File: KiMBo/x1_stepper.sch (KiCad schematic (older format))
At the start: 23 parts, among them U25 TMC2130

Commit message: Arrange connectors and E-stepper circuit
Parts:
- R193: footprint Resistors_SMD:R_0805 -> Resistors_SMD:R_0603
- R195: footprint Resistors_SMD:R_0603 -> Resistors_SMD:R_0805
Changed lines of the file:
@@
 F 0 "R195" H 10700 6650 50  0000 R CNN
 F 1 "220mΩ" H 10700 6750 50  0000 R CNN
-F 2 "Resistors_SMD:R_0603" V 10680 6700 50  0001 C CNN
+F 2 "Resistors_SMD:R_0805" V 10680 6700 50  0001 C CNN
 F 3 "" H 10750 6700 50  0000 C CNN
 	1    10750 6700
@@
 F 0 "R193" V 9250 6900 50  0000 C CNN
 F 1 "4.75kΩ" V 9350 6900 50  0000 C CNN
-F 2 "Resistors_SMD:R_0805" V 9380 6900 50  0001 C CNN
+F 2 "Resistors_SMD:R_0603" V 9380 6900 50  0001 C CNN
 F 3 "" H 9450 6900 50  0000 C CNN
 	1    9450 6900

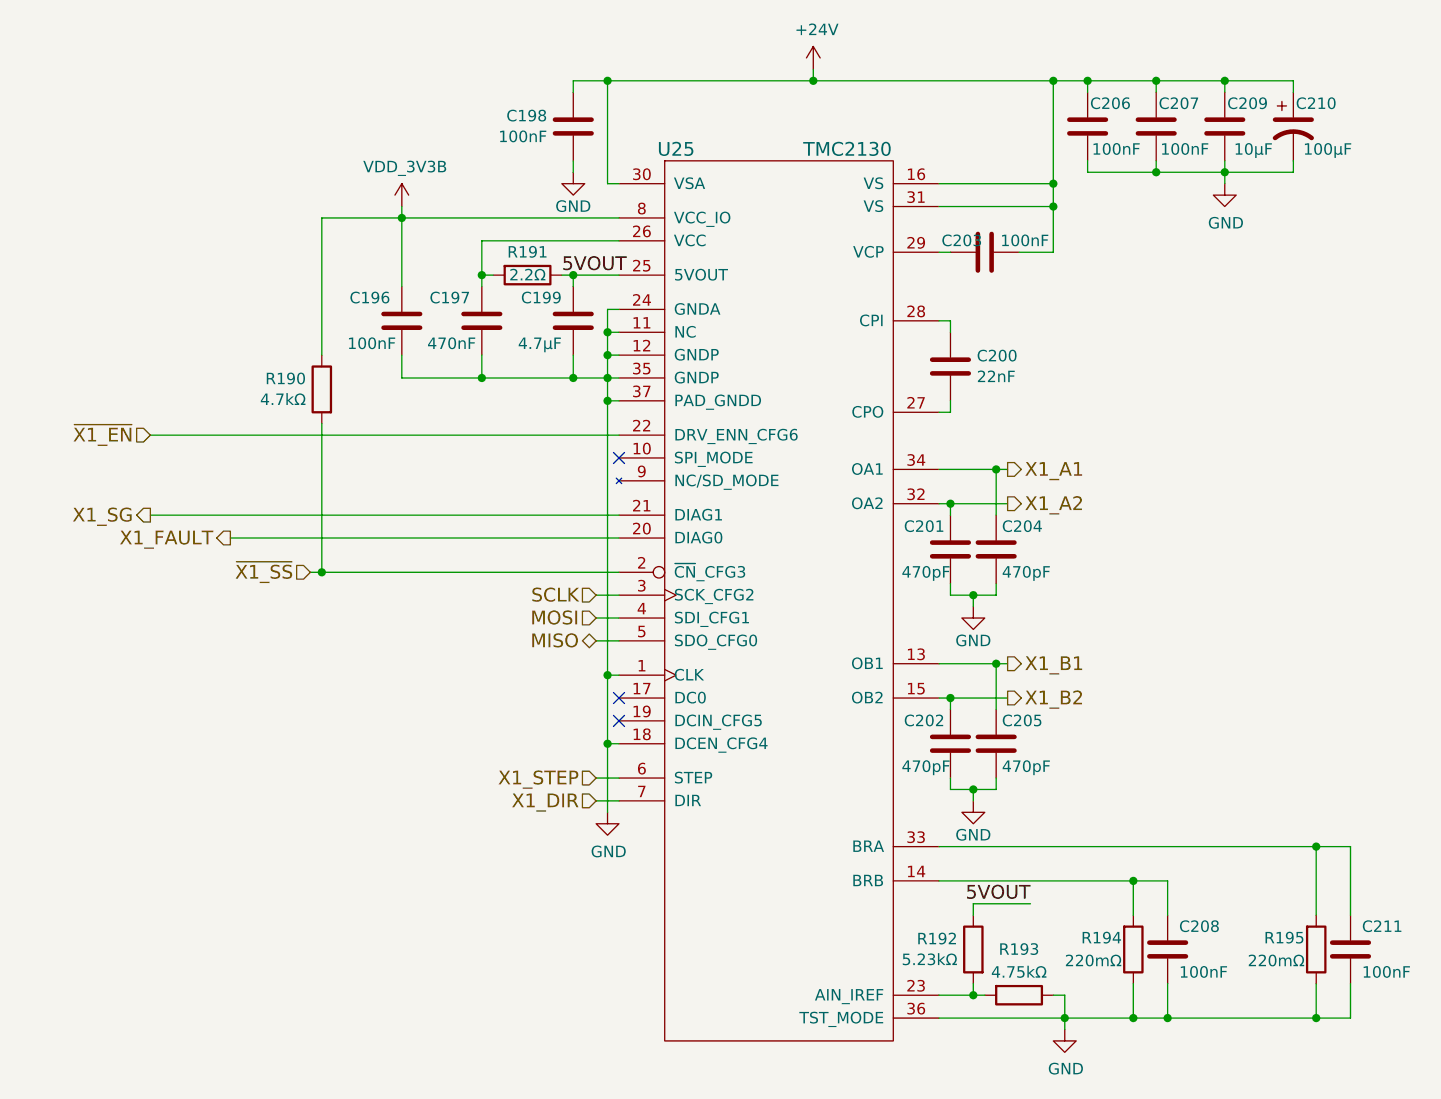
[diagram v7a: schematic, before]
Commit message: Remove HDMI from the schematic
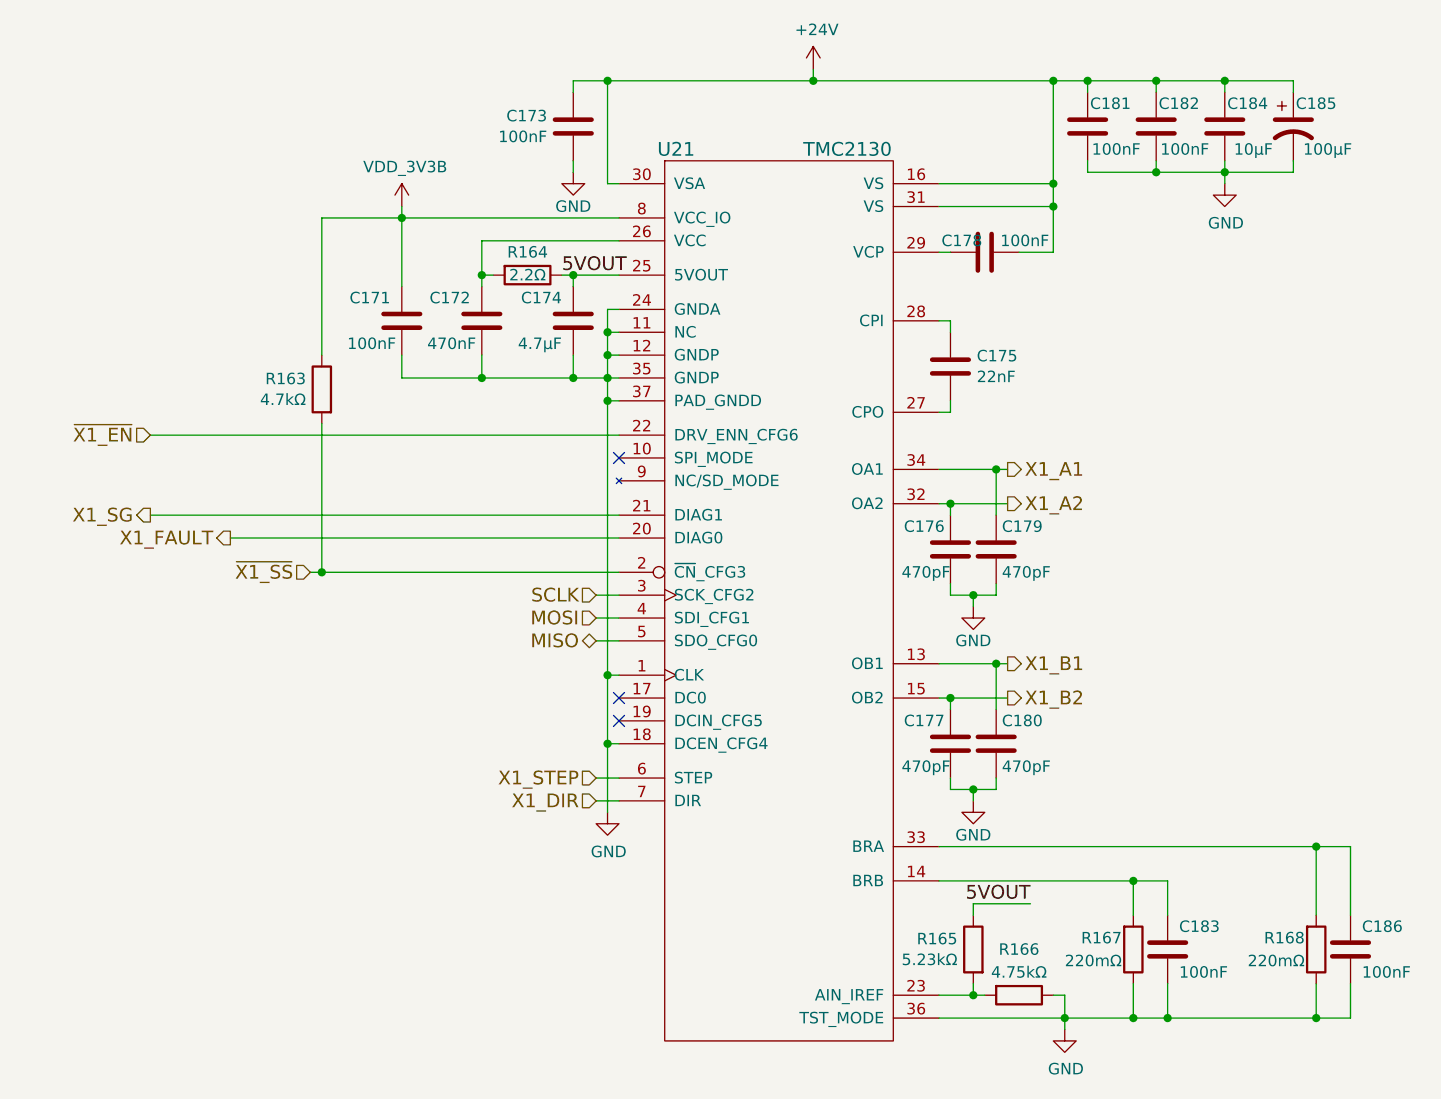
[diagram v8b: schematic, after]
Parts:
- renumbered C196 to C171, C197 to C172, C198 to C173, C199 to C174, C200 to C175, C201 to C176, C202 to C177, C203 to C178, C204 to C179, C205 to C180, C206 to C181, C207 to C182, C208 to C183, C209 to C184, C210 to C185, C211 to C186, R190 to R163, R191 to R164, R192 to R165, R193 to R166, R194 to R167, R195 to R168, U25 to U21
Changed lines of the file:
@@
 $Descr A3 16535 11693
 encoding utf-8
-Sheet 23 26
+Sheet 23 25
 Title ""
 Date ""
@@
 X1_SG
 $Comp
-L C C198
+L C C173
 U 1 1 58C092B6
 P 7500 3100
-F 0 "C198" H 7386 3054 50  0000 R CNN
+F 0 "C173" H 7386 3054 50  0000 R CNN
 F 1 "100nF" H 7386 3145 50  0000 R CNN
 F 2 "Capacitors_SMD:C_0603" H 7538 2950 50  0001 C CNN
@@
 $EndComp
 $Comp
-L C C203
+L C C178
 U 1 1 58C092BD
 P 9300 3650
-F 0 "C203" V 9250 3550 50  0000 C CNN
+F 0 "C178" V 9250 3550 50  0000 C CNN
 F 1 "100nF" V 9250 3825 50  0000 C CNN
 F 2 "Capacitors_SMD:C_0603" H 9338 3500 50  0001 C CNN
@@
 $EndComp
 $Comp
-L CP1 C210
+L CP1 C185
 U 1 1 5BA7E13D
 P 10650 3100
-F 0 "C210" H 10750 3200 50  0000 C CNN
+F 0 "C185" H 10750 3200 50  0000 C CNN
 F 1 "100μF" H 10800 3000 50  0000 C CNN
 F 2 "Capacitors_SMD:c_elec_8x10" H 10650 3100 50  0001 C CNN
@@
 $EndComp
 $Comp
-L C C206
+L C C181
 U 1 1 5BA7E13E
 P 9750 3100
-F 0 "C206" H 9650 3200 50  0000 C CNN
+F 0 "C181" H 9650 3200 50  0000 C CNN
 F 1 "100nF" H 9625 3000 50  0000 C CNN
 F 2 "Capacitors_SMD:C_0603" H 9788 2950 50  0001 C CNN
@@
 $EndComp
 $Comp
-L GND #PWR0256
+L GND #PWR0225
 U 1 1 5BA7E13F
 P 7500 3300
-F 0 "#PWR0256" H 7500 3050 50  0001 C CNN
+F 0 "#PWR0225" H 7500 3050 50  0001 C CNN
 F 1 "GND" H 7500 3150 50  0000 C CNN
 F 2 "" H 7500 3300 50  0000 C CNN
@@
 $EndComp
 $Comp
-L C C207
+L C C182
 U 1 1 58C092D8
 P 10050 3100
-F 0 "C207" H 9950 3200 50  0000 C CNN
+F 0 "C182" H 9950 3200 50  0000 C CNN
 F 1 "100nF" H 9925 3000 50  0000 C CNN
 F 2 "Capacitors_SMD:C_0603" H 10088 2950 50  0001 C CNN
@@
 $EndComp
 $Comp
-L GND #PWR0257
+L GND #PWR0226
 U 1 1 58C092DF
 P 10350 3350
-F 0 "#PWR0257" H 10350 3100 50  0001 C CNN
+F 0 "#PWR0226" H 10350 3100 50  0001 C CNN
 F 1 "GND" H 10355 3177 50  0000 C CNN
 F 2 "" H 10350 3350 50  0000 C CNN
@@
 $EndComp
 $Comp
-L +24V #PWR0258
+L +24V #PWR0227
 U 1 1 5BA7E142
 P 8550 2850
-F 0 "#PWR0258" H 8550 2700 50  0001 C CNN
+F 0 "#PWR0227" H 8550 2700 50  0001 C CNN
 F 1 "+24V" H 8565 3023 50  0000 C CNN
 F 2 "" H 8550 2850 50  0000 C CNN
@@
 $EndComp
 $Comp
-L C C200
+L C C175
 U 1 1 5BA7E143
 P 9150 4150
-F 0 "C200" H 9265 4196 50  0000 L CNN
+F 0 "C175" H 9265 4196 50  0000 L CNN
 F 1 "22nF" H 9265 4105 50  0000 L CNN
 F 2 "Capacitors_SMD:C_0603" H 9188 4000 50  0001 C CNN
@@
 $EndComp
 $Comp
-L R R195
+L R R168
 U 1 1 5BA7E144
 P 10750 6700
-F 0 "R195" H 10700 6650 50  0000 R CNN
+F 0 "R168" H 10700 6650 50  0000 R CNN
 F 1 "220mΩ" H 10700 6750 50  0000 R CNN
 F 2 "Resistors_SMD:R_0805" V 10680 6700 50  0001 C CNN
@@
 $EndComp
 $Comp
-L R R194
+L R R167
 U 1 1 5BA7E145
 P 9950 6700
-F 0 "R194" H 9900 6650 50  0000 R CNN
+F 0 "R167" H 9900 6650 50  0000 R CNN
 F 1 "220mΩ" H 9900 6750 50  0000 R CNN
 F 2 "Resistors_SMD:R_0805" V 9880 6700 50  0001 C CNN
@@
 $EndComp
 $Comp
-L GND #PWR0259
+L GND #PWR0228
 U 1 1 58C09300
 P 9650 7050
-F 0 "#PWR0259" H 9650 6800 50  0001 C CNN
+F 0 "#PWR0228" H 9650 6800 50  0001 C CNN
 F 1 "GND" H 9655 6877 50  0000 C CNN
 F 2 "" H 9650 7050 50  0000 C CNN
@@
 NoConn ~ 7700 5600
 $Comp
-L R R191
+L R R164
 U 1 1 58C09307
 P 7300 3750
-F 0 "R191" V 7200 3750 50  0000 C CNN
+F 0 "R164" V 7200 3750 50  0000 C CNN
 F 1 "2.2Ω" V 7300 3750 50  0000 C CNN
 F 2 "Resistors_SMD:R_0603" V 7230 3750 50  0001 C CNN
@@
 $EndComp
 $Comp
-L C C197
+L C C172
 U 1 1 58C0930E
 P 7100 3950
-F 0 "C197" H 7150 4050 50  0000 L CNN
+F 0 "C172" H 7150 4050 50  0000 L CNN
 F 1 "470nF" H 7125 3850 50  0000 L CNN
 F 2 "Capacitors_SMD:C_0603" H 7138 3800 50  0001 C CNN
@@
 NoConn ~ 7700 5700
 $Comp
-L GND #PWR0260
+L GND #PWR0229
 U 1 1 58C09323
 P 7650 6100
-F 0 "#PWR0260" H 7650 5850 50  0001 C CNN
+F 0 "#PWR0229" H 7650 5850 50  0001 C CNN
 F 1 "GND" H 7655 5927 50  0000 C CNN
 F 2 "" H 7650 6100 50  0000 C CNN
@@
 $EndComp
 $Comp
-L C C208
+L C C183
 U 1 1 58C09329
 P 10100 6700
-F 0 "C208" H 10150 6800 50  0000 L CNN
+F 0 "C183" H 10150 6800 50  0000 L CNN
 F 1 "100nF" H 10150 6600 50  0000 L CNN
 F 2 "Capacitors_SMD:C_0603" H 10138 6550 50  0001 C CNN
@@
 NoConn ~ 7700 4550
 $Comp
-L C C199
+L C C174
 U 1 1 58C0933B
 P 7500 3950
-F 0 "C199" H 7550 4050 50  0000 L CNN
+F 0 "C174" H 7550 4050 50  0000 L CNN
 F 1 "4.7μF" H 7550 3850 50  0000 L CNN
 F 2 "Capacitors_SMD:C_0603" H 7538 3800 50  0001 C CNN
@@
 5VOUT
 $Comp
-L R R192
+L R R165
 U 1 1 58C09343
 P 9250 6700
-F 0 "R192" H 9319 6746 50  0000 L CNN
+F 0 "R165" H 9319 6746 50  0000 L CNN
 F 1 "5.23kΩ" H 9319 6655 50  0000 L CNN
 F 2 "Resistors_SMD:R_0603" V 9180 6700 50  0001 C CNN
@@
 5VOUT
 $Comp
-L R R193
+L R R166
 U 1 1 58C0934B
 P 9450 6900
-F 0 "R193" V 9250 6900 50  0000 C CNN
+F 0 "R166" V 9250 6900 50  0000 C CNN
 F 1 "4.75kΩ" V 9350 6900 50  0000 C CNN
 F 2 "Resistors_SMD:R_0603" V 9380 6900 50  0001 C CNN
@@
 $EndComp
 $Comp
-L R R190
+L R R163
 U 1 1 5BA7E14F
 P 6400 4250
-F 0 "R190" H 6469 4296 50  0000 L CNN
+F 0 "R163" H 6469 4296 50  0000 L CNN
 F 1 "4.7kΩ" H 6469 4205 50  0000 L CNN
 F 2 "Resistors_SMD:R_0603" V 6330 4250 50  0001 C CNN
@@
 $EndComp
 $Comp
-L C C211
+L C C186
 U 1 1 5BA7E150
 P 10900 6700
-F 0 "C211" H 10950 6800 50  0000 L CNN
+F 0 "C186" H 10950 6800 50  0000 L CNN
 F 1 "100nF" H 10950 6600 50  0000 L CNN
 F 2 "Capacitors_SMD:C_0603" H 10938 6550 50  0001 C CNN
@@
 $EndComp
 $Comp
-L C C201
+L C C176
 U 1 1 5BA7E151
 P 9150 4950
-F 0 "C201" H 9175 5050 50  0000 L CNN
+F 0 "C176" H 9175 5050 50  0000 L CNN
 F 1 "470pF" H 9150 4850 50  0000 L CNN
 F 2 "Capacitors_SMD:C_0603" H 9188 4800 50  0001 C CNN
@@
 $EndComp
 $Comp
-L GND #PWR0261
+L GND #PWR0230
 U 1 1 5BA7E152
 P 9250 5200
-F 0 "#PWR0261" H 9250 4950 50  0001 C CNN
+F 0 "#PWR0230" H 9250 4950 50  0001 C CNN
 F 1 "GND" H 9250 5050 50  0000 C CNN
 F 2 "" H 9250 5200 50  0000 C CNN
@@
 $EndComp
 $Comp
-L C C204
+L C C179
 U 1 1 5BA7E153
 P 9350 4950
-F 0 "C204" H 9375 5050 50  0000 L CNN
+F 0 "C179" H 9375 5050 50  0000 L CNN
 F 1 "470pF" H 9375 4850 50  0000 L CNN
 F 2 "Capacitors_SMD:C_0603" H 9388 4800 50  0001 C CNN
@@
 $EndComp
 $Comp
-L C C202
+L C C177
 U 1 1 58C09377
 P 9150 5800
-F 0 "C202" H 9175 5900 50  0000 L CNN
+F 0 "C177" H 9175 5900 50  0000 L CNN
 F 1 "470pF" H 9150 5700 50  0000 L CNN
 F 2 "Capacitors_SMD:C_0603" H 9188 5650 50  0001 C CNN
@@
 $EndComp
 $Comp
-L GND #PWR0262
+L GND #PWR0231
 U 1 1 5BA7E155
 P 9250 6050
-F 0 "#PWR0262" H 9250 5800 50  0001 C CNN
+F 0 "#PWR0231" H 9250 5800 50  0001 C CNN
 F 1 "GND" H 9250 5900 50  0000 C CNN
 F 2 "" H 9250 6050 50  0000 C CNN
@@
 $EndComp
 $Comp
-L C C205
+L C C180
 U 1 1 5BA7E156
 P 9350 5800
-F 0 "C205" H 9375 5900 50  0000 L CNN
+F 0 "C180" H 9375 5900 50  0000 L CNN
 F 1 "470pF" H 9375 5700 50  0000 L CNN
 F 2 "Capacitors_SMD:C_0603" H 9388 5650 50  0001 C CNN
@@
 $EndComp
 $Comp
-L TMC2130 U25
+L TMC2130 U21
 U 1 1 5BA7E157
 P 8400 4700
-F 0 "U25" H 7950 6200 60  0000 C CNN
+F 0 "U21" H 7950 6200 60  0000 C CNN
 F 1 "TMC2130" H 8700 6200 60  0000 C CNN
 F 2 "KiMBo:QFN36_5X6" H 8400 5000 60  0001 C CNN
@@
 	9150 6000 9150 5950
 $Comp
-L C C209
+L C C184
 U 1 1 58C0940A
 P 10350 3100
-F 0 "C209" H 10250 3200 50  0000 C CNN
+F 0 "C184" H 10250 3200 50  0000 C CNN
 F 1 "10μF" H 10225 3000 50  0000 C CNN
 F 2 "Capacitors_SMD:C_0805" H 10388 2950 50  0001 C CNN
@@
 	6400 3500 7700 3500
 $Comp
-L VDD_3V3B #PWR0263
+L VDD_3V3B #PWR0232
 U 1 1 5BA7E15A
 P 6750 3450
-F 0 "#PWR0263" H 6750 3300 50  0001 C CNN
+F 0 "#PWR0232" H 6750 3300 50  0001 C CNN
 F 1 "VDD_3V3B" H 6765 3623 50  0000 C CNN
 F 2 "" H 6750 3450 50  0000 C CNN
@@
 $EndComp
 $Comp
-L C C196
+L C C171
 U 1 1 5A89A0A1
 P 6750 3950
-F 0 "C196" H 6800 4050 50  0000 L CNN
+F 0 "C171" H 6800 4050 50  0000 L CNN
 F 1 "100nF" H 6775 3850 50  0000 L CNN
 F 2 "Capacitors_SMD:C_0603" H 6788 3800 50  0001 C CNN
